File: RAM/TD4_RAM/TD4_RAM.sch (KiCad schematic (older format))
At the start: 0 parts

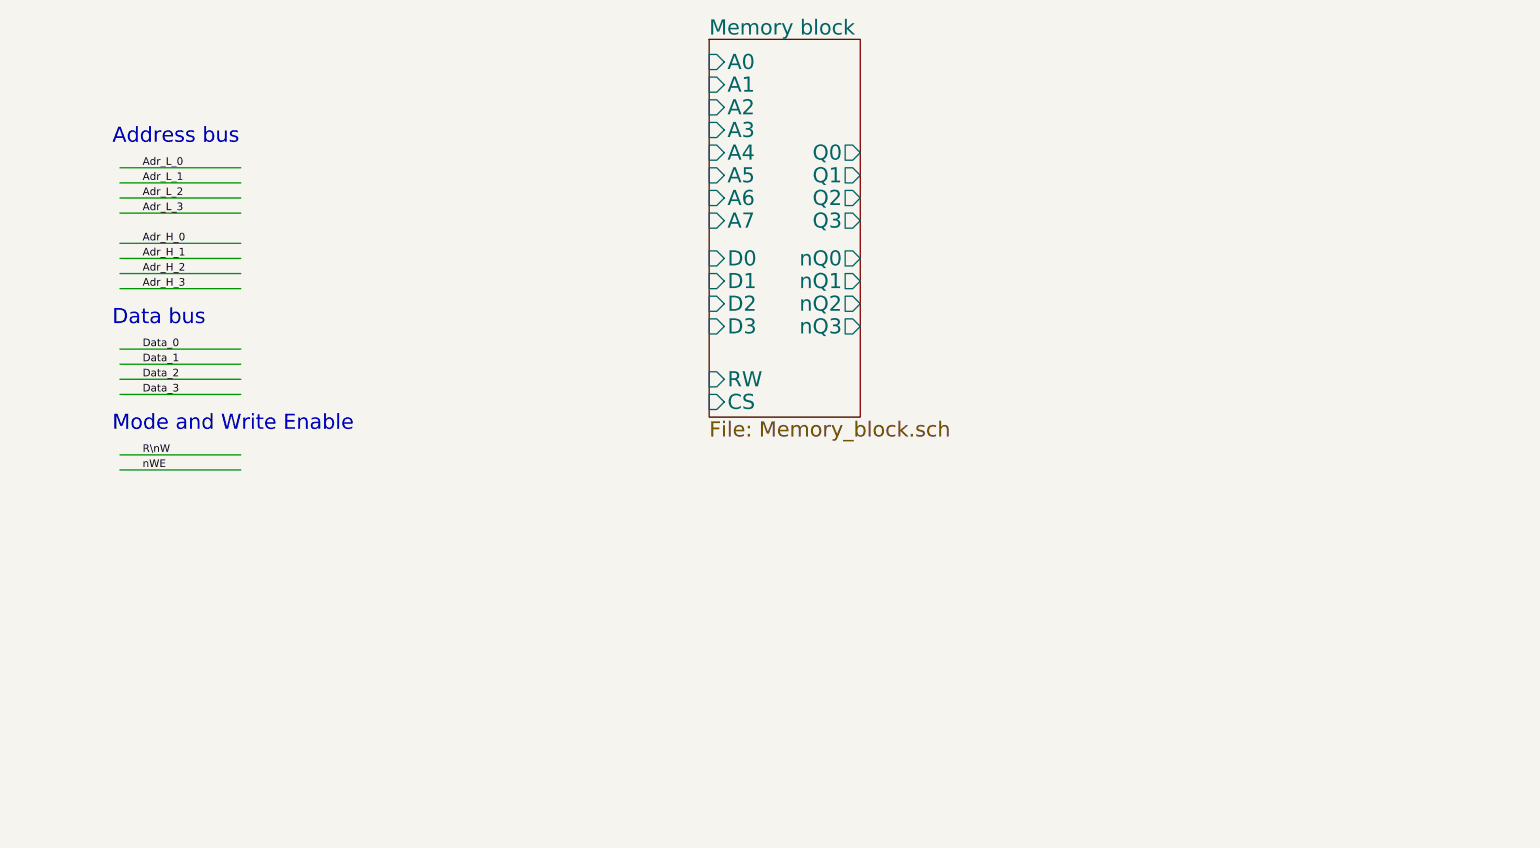
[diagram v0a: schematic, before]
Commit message: Address decoder done
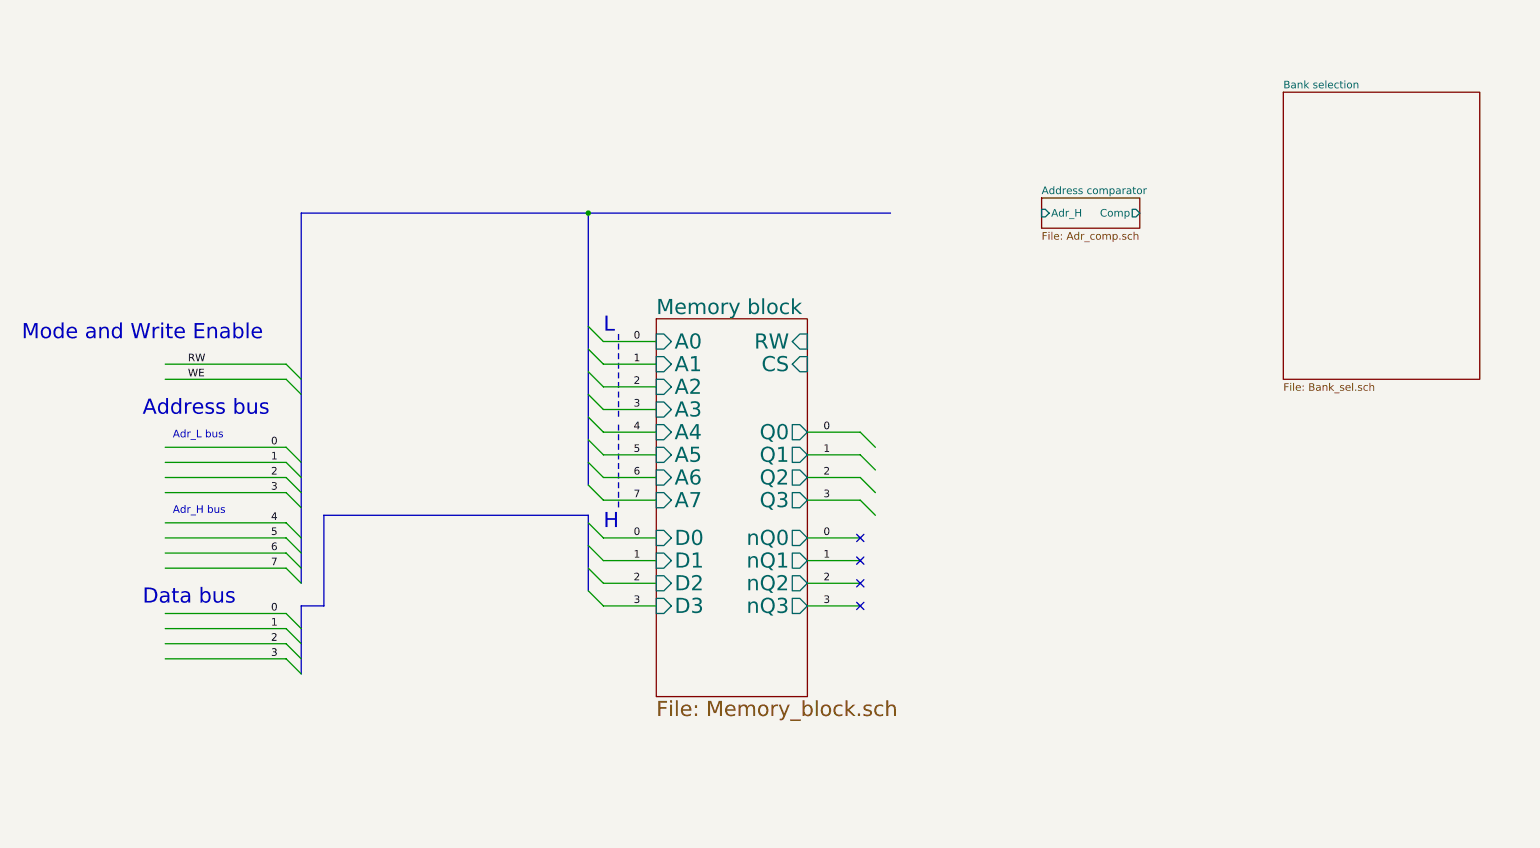
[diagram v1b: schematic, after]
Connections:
- net labels added: 0, 1, 2, 3, 4, 5, 6, 7, RW, WE
- net labels removed: Adr_H_0, Adr_H_1, Adr_H_2, Adr_H_3, Adr_L_0, Adr_L_1, Adr_L_2, Adr_L_3, Data_0, Data_1, Data_2, Data_3, R\nW, nWE
- wire segments 14 -> 34
- no-connect marks 0 -> 4
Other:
- note added: "Adr_H bus"
- note added: "Adr_L bus"
- note added: "H"
- note added: "L"

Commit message: RAM done (sort of)
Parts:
- added U?: 74AHC1G32, symbol 74xGxx:74AHC1G32
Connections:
- net labels added: GND, VCC, nWE
- net labels removed: WE
- wire segments 34 -> 45
- no-connect marks 4 -> 0

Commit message: RAM refactoring goes on
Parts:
- gave numbers to parts that had none: 1
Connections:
- net labels added: A[0..7], D[0..4], t0, t1, t2, t3, t[0..3], ~WE
- net labels removed: 0, 1, 2, 3, nWE
- wire segments 45 -> 11
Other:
- note removed: "Adr_H bus"
- note removed: "Adr_L bus"
- note removed: "H"
- note removed: "L"
- moved on the sheet: U1

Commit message: RAM done (damn buses\!)
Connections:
- net labels added: A0, A1, A2, A3, A4, A5, A6, A7, D0, D1, D2, D3
- net labels removed: 4, 5, 6, 7
- wire segments 11 -> 23
- no-connect marks 0 -> 14
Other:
- moved on the sheet: U1

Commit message: Decoder done (finally!)
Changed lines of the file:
@@
 U 5CBF05D8
 F0 "sheet5CBF05D4" 50
-F1 "Bank_witches.sch" 50
+F1 "Bank_switches.sch" 50
 F2 "Out[0..15]" O R 4900 1700 50
 $EndSheet
@@
 NoConn ~ 950  4900
 NoConn ~ 950  3150
+NoConn ~ 950  3250
 Wire Bus Line
 	1250 3650 4400 3650
@@
 Wire Bus Line
 	1250 3650 1250 4400
-NoConn ~ 950  3250
 $EndSCHEMATC

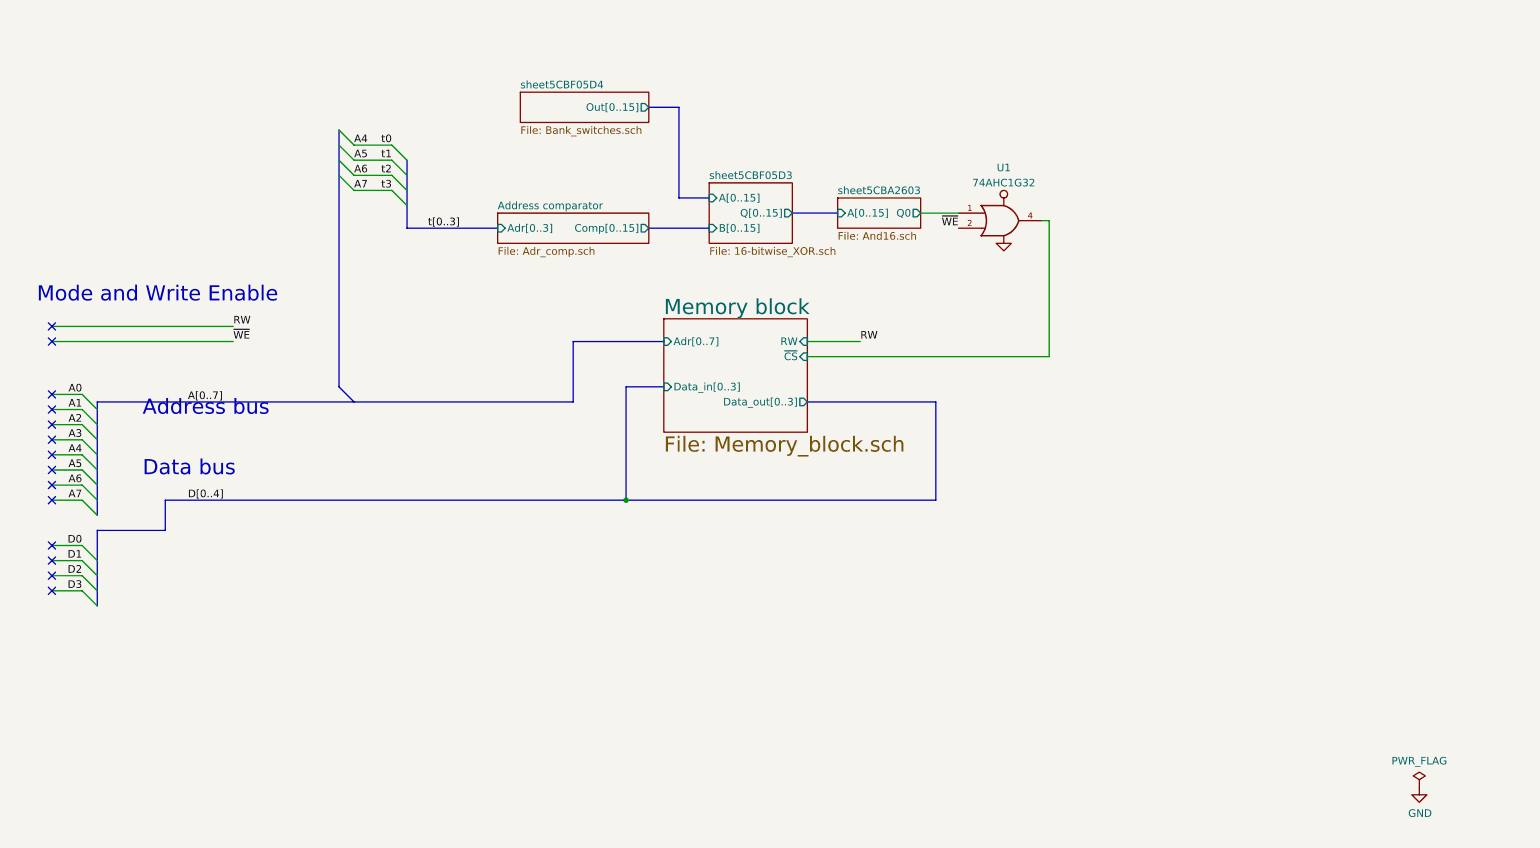
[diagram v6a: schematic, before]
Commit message: Added backplane connectors to all PCBs
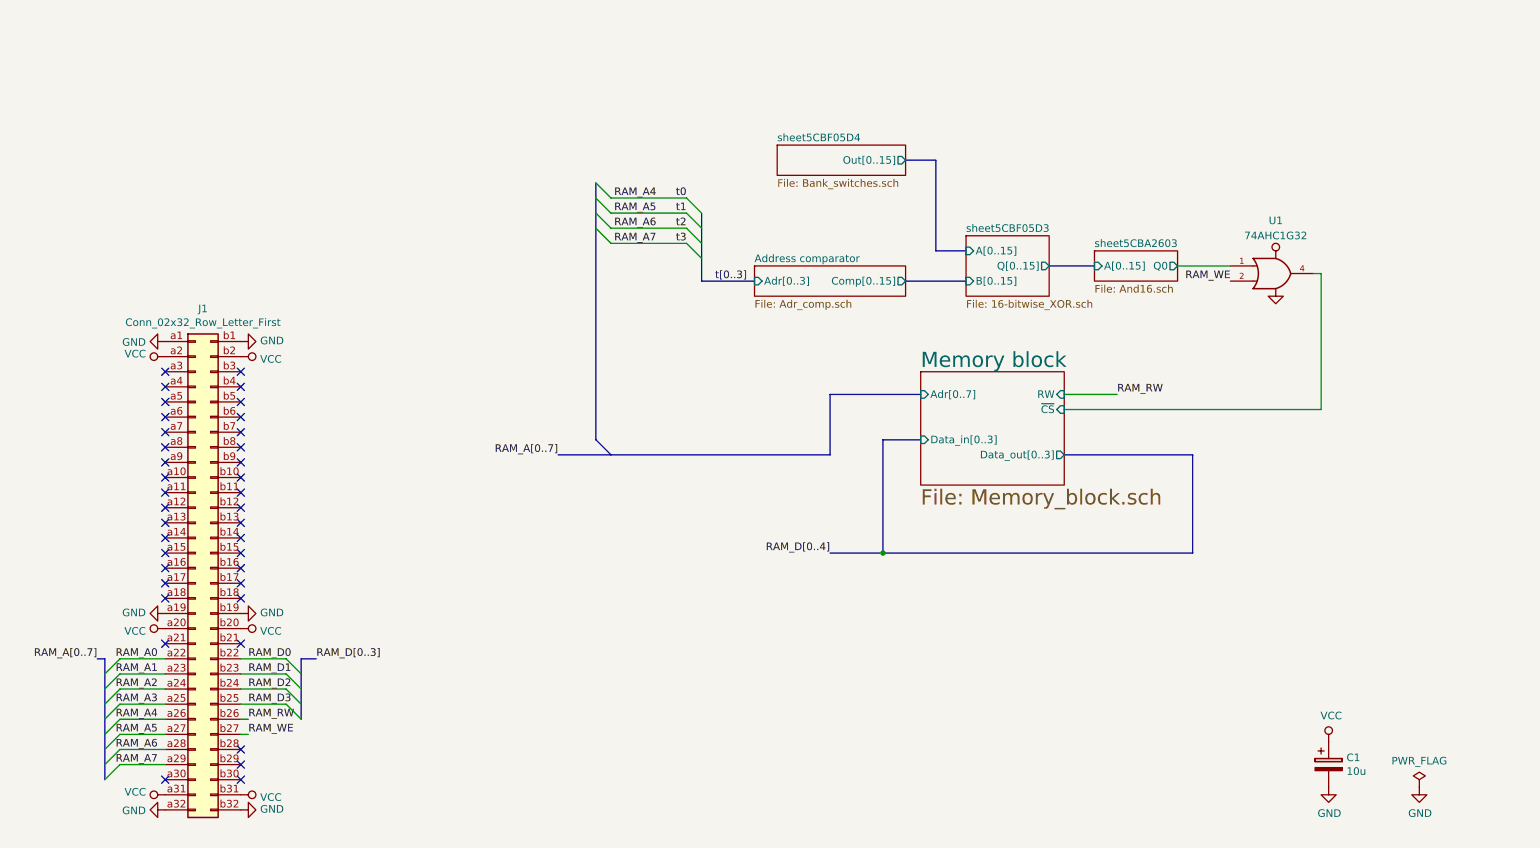
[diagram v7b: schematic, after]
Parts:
- added C1: 10u, Capacitor_Tantalum_SMD:CP_EIA-3216-18_Kemet-A, symbol Device:CP
- added J1: Conn_02x32_Row_Letter_First, Connector_DIN:DIN41612_B_2x32_Horizontal, symbol Connector_Generic:Conn_02x32_Row_Letter_First
- U1: footprint (none) -> Package_TO_SOT_SMD:SOT-23-5
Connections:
- net GND: now also C1.2, J1.a1 (Pin_a1), J1.a19 (Pin_a19), J1.a32 (Pin_a32), J1.b1 (Pin_b1), J1.b19 (Pin_b19), J1.b32 (Pin_b32)
- net VCC: now also C1.1, J1.a2 (Pin_a2), J1.a20 (Pin_a20), J1.a31 (Pin_a31), J1.b2 (Pin_b2), J1.b20 (Pin_b20), J1.b31 (Pin_b31)
- net ~WE renamed RAM_WE
- net RAM_WE: now also J1.b27 (Pin_b27)
- new net RAM_A0: J1.a22 (Pin_a22)
- new net RAM_A1: J1.a23 (Pin_a23)
- new net RAM_A2: J1.a24 (Pin_a24)
- new net RAM_A3: J1.a25 (Pin_a25)
- new net RAM_A4: J1.a26 (Pin_a26)
- new net RAM_A5: J1.a27 (Pin_a27)
- new net RAM_A6: J1.a28 (Pin_a28)
- new net RAM_A7: J1.a29 (Pin_a29)
- new net RAM_D0: J1.b22 (Pin_b22)
- new net RAM_D1: J1.b23 (Pin_b23)
- new net RAM_D2: J1.b24 (Pin_b24)
- new net RAM_D3: J1.b25 (Pin_b25)
- new net RAM_RW: J1.b26 (Pin_b26)
- no-connect marks 14 -> 38
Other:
- note removed: "Address bus"
- note removed: "Data bus"
- note removed: "Mode and Write Enable"
- moved on the sheet: U1

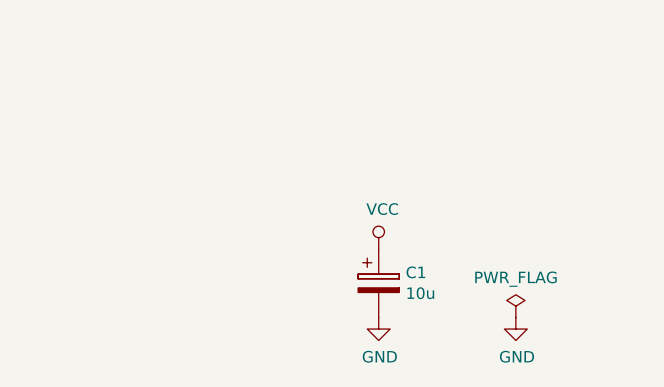
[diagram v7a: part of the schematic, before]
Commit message: Main RAM blocks routed
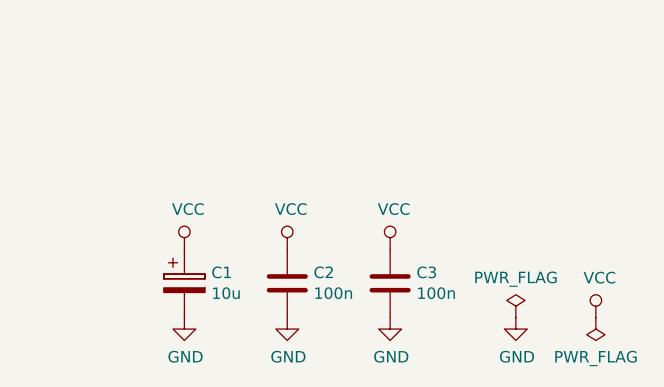
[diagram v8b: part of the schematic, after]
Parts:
- added C2, C3: 100n, Capacitor_SMD:C_0805_2012Metric, symbol Device:C
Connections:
- net GND: now also C2.2, C3.2
- net VCC: now also C2.1, C3.1
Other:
- moved on the sheet: C1
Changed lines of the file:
@@
 $EndComp
 $Comp
-L power:GND #PWR013
+L power:GND #PWR017
 U 1 1 5C5F6284
 P 10000 6200
-F 0 "#PWR013" H 10000 5950 50  0001 C CNN
+F 0 "#PWR017" H 10000 5950 50  0001 C CNN
 F 1 "GND" H 10005 6027 50  0000 C CNN
 F 2 "" H 10000 6200 50  0001 C CNN
@@
 $EndComp
 $Comp
-L power:GND #PWR016
+L power:GND #PWR021
 U 1 1 5C90856C
 P 1700 6350
-F 0 "#PWR016" H 1700 6100 50  0001 C CNN
+F 0 "#PWR021" H 1700 6100 50  0001 C CNN
 F 1 "GND" V 1705 6222 50  0000 R CNN
 F 2 "" H 1700 6350 50  0001 C CNN
@@
 $EndComp
 $Comp
-L power:GND #PWR017
+L power:GND #PWR022
 U 1 1 5C90857E
 P 2200 6350
-F 0 "#PWR017" H 2200 6100 50  0001 C CNN
+F 0 "#PWR022" H 2200 6100 50  0001 C CNN
 F 1 "GND" V 2205 6222 50  0000 R CNN
 F 2 "" H 2200 6350 50  0001 C CNN
@@
 $EndComp
 $Comp
-L power:VCC #PWR015
+L power:VCC #PWR020
 U 1 1 5C908584
 P 2200 6250
-F 0 "#PWR015" H 2200 6100 50  0001 C CNN
+F 0 "#PWR020" H 2200 6100 50  0001 C CNN
 F 1 "VCC" V 2217 6378 50  0000 L CNN
 F 2 "" H 2200 6250 50  0001 C CNN
@@
 $EndComp
 $Comp
-L power:VCC #PWR014
+L power:VCC #PWR019
 U 1 1 5C908596
 P 1700 6250
-F 0 "#PWR014" H 1700 6100 50  0001 C CNN
+F 0 "#PWR019" H 1700 6100 50  0001 C CNN
 F 1 "VCC" V 1718 6377 50  0000 L CNN
 F 2 "" H 1700 6250 50  0001 C CNN
@@
 L Device:CP C1
 U 1 1 5C6E5845
-P 9400 6050
-F 0 "C1" H 9518 6096 50  0000 L CNN
-F 1 "10u" H 9518 6005 50  0000 L CNN
-F 2 "Capacitor_Tantalum_SMD:CP_EIA-3216-18_Kemet-A" H 9438 5900 50  0001 C CNN
-F 3 "~" H 9400 6050 50  0001 C CNN
-	1    9400 6050
-	1    0    0    -1
-$EndComp
-$Comp
-L power:GND #PWR012
+P 8550 6050
+F 0 "C1" H 8668 6096 50  0000 L CNN
+F 1 "10u" H 8668 6005 50  0000 L CNN
+F 2 "Capacitor_Tantalum_SMD:CP_EIA-3216-18_Kemet-A" H 8588 5900 50  0001 C CNN
+F 3 "~" H 8550 6050 50  0001 C CNN
+	1    8550 6050
+	1    0    0    -1
+$EndComp
+$Comp
+L power:GND #PWR014
 U 1 1 5C6E58AC
-P 9400 6200
-F 0 "#PWR012" H 9400 5950 50  0001 C CNN
-F 1 "GND" H 9405 6027 50  0000 C CNN
-F 2 "" H 9400 6200 50  0001 C CNN
-F 3 "" H 9400 6200 50  0001 C CNN
-	1    9400 6200
+P 8550 6200
+F 0 "#PWR014" H 8550 5950 50  0001 C CNN
+F 1 "GND" H 8555 6027 50  0000 C CNN
+F 2 "" H 8550 6200 50  0001 C CNN
+F 3 "" H 8550 6200 50  0001 C CNN
+	1    8550 6200
 	1    0    0    -1
 $EndComp
@@
 L power:VCC #PWR011
 U 1 1 5C6E5901
-P 9400 5900
-F 0 "#PWR011" H 9400 5750 50  0001 C CNN
-F 1 "VCC" H 9417 6073 50  0000 C CNN
-F 2 "" H 9400 5900 50  0001 C CNN
-F 3 "" H 9400 5900 50  0001 C CNN
-	1    9400 5900
-	1    0    0    -1
-$EndComp
+P 8550 5900
+F 0 "#PWR011" H 8550 5750 50  0001 C CNN
+F 1 "VCC" H 8567 6073 50  0000 C CNN
+F 2 "" H 8550 5900 50  0001 C CNN
+F 3 "" H 8550 5900 50  0001 C CNN
+	1    8550 5900
+	1    0    0    -1
+$EndComp
+$Comp
+L Device:C C2
+U 1 1 5C70A92B
+P 9000 6050
+F 0 "C2" H 9115 6096 50  0000 L CNN
+F 1 "100n" H 9115 6005 50  0000 L CNN
+F 2 "Capacitor_SMD:C_0805_2012Metric" H 9038 5900 50  0001 C CNN
+F 3 "~" H 9000 6050 50  0001 C CNN
+	1    9000 6050
+	1    0    0    -1
+$EndComp
+$Comp
+L power:VCC #PWR012
+U 1 1 5C70A991
+P 9000 5900
+F 0 "#PWR012" H 9000 5750 50  0001 C CNN
+F 1 "VCC" H 9017 6073 50  0000 C CNN
+F 2 "" H 9000 5900 50  0001 C CNN
+F 3 "" H 9000 5900 50  0001 C CNN
+	1    9000 5900
+	1    0    0    -1
+$EndComp
+$Comp
+L power:GND #PWR015
+U 1 1 5C70A9D4
+P 9000 6200
+F 0 "#PWR015" H 9000 5950 50  0001 C CNN
+F 1 "GND" H 9005 6027 50  0000 C CNN
+F 2 "" H 9000 6200 50  0001 C CNN
+F 3 "" H 9000 6200 50  0001 C CNN
+	1    9000 6200
+	1    0    0    -1
+$EndComp
+$Comp
+L power:VCC #PWR018
+U 1 1 5C719C25
+P 10350 6200
+F 0 "#PWR018" H 10350 6050 50  0001 C CNN
+F 1 "VCC" H 10367 6373 50  0000 C CNN
+F 2 "" H 10350 6200 50  0001 C CNN
+F 3 "" H 10350 6200 50  0001 C CNN
+	1    10350 6200
+	1    0    0    -1
+$EndComp
+$Comp
+L power:PWR_FLAG #FLG02
+U 1 1 5C719C6F
+P 10350 6200
+F 0 "#FLG02" H 10350 6275 50  0001 C CNN
+F 1 "PWR_FLAG" H 10350 6373 50  0000 C CNN
+F 2 "" H 10350 6200 50  0001 C CNN
+F 3 "~" H 10350 6200 50  0001 C CNN
+	1    10350 6200
+	-1   0    0    1
+$EndComp
+$Comp
+L Device:C C3
+U 1 1 5C71B511
+P 9450 6050
+F 0 "C3" H 9565 6096 50  0000 L CNN
+F 1 "100n" H 9565 6005 50  0000 L CNN
+F 2 "Capacitor_SMD:C_0805_2012Metric" H 9488 5900 50  0001 C CNN
+F 3 "~" H 9450 6050 50  0001 C CNN
+	1    9450 6050
+	1    0    0    -1
+$EndComp
+$Comp
+L power:VCC #PWR013
+U 1 1 5C71B518
+P 9450 5900
+F 0 "#PWR013" H 9450 5750 50  0001 C CNN
+F 1 "VCC" H 9467 6073 50  0000 C CNN
+F 2 "" H 9450 5900 50  0001 C CNN
+F 3 "" H 9450 5900 50  0001 C CNN
+	1    9450 5900
+	1    0    0    -1
+$EndComp
+$Comp
+L power:GND #PWR016
+U 1 1 5C71B51E
+P 9450 6200
+F 0 "#PWR016" H 9450 5950 50  0001 C CNN
+F 1 "GND" H 9455 6027 50  0000 C CNN
+F 2 "" H 9450 6200 50  0001 C CNN
+F 3 "" H 9450 6200 50  0001 C CNN
+	1    9450 6200
+	1    0    0    -1
+$EndComp
